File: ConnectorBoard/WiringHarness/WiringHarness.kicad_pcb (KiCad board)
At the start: 2 copper layers, 56.9 x 31.5 mm, 15 parts, among them J1 Barrel_Jack, J2 Conn_01x03, J3 Conn_01x03, J4 Conn_02x05_Odd_Even, U1 L7805, U2 L7805

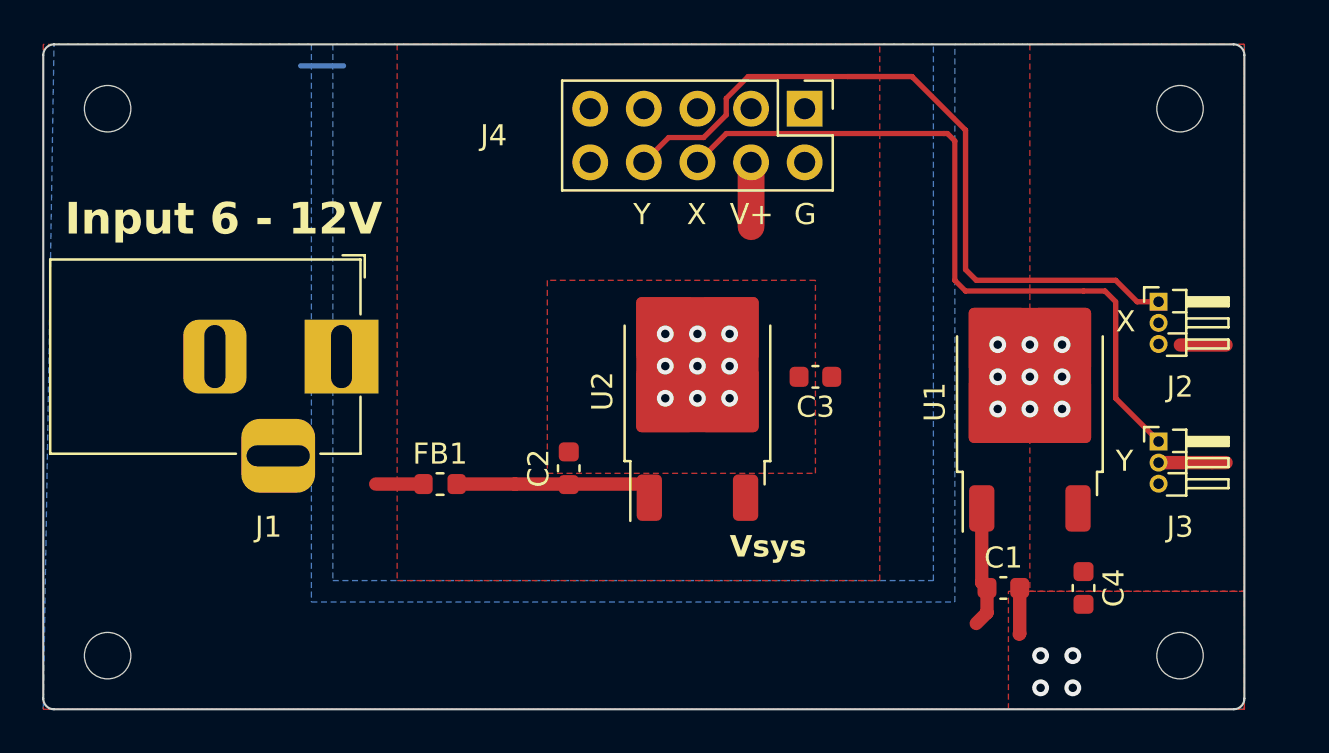
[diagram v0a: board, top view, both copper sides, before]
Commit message: Add right angle ribbon cable to wiring harness
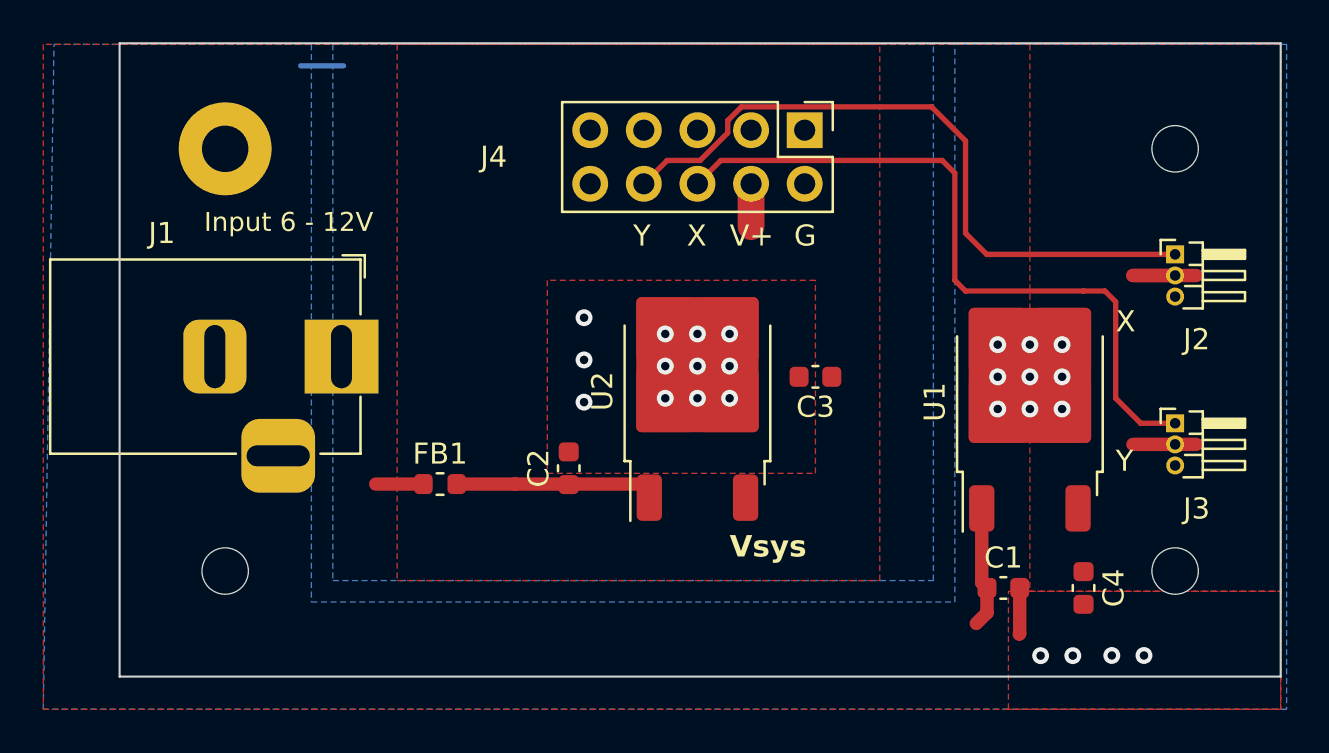
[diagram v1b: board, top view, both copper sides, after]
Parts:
- removed H1: MountingHole, MountingHole:MountingHole_2.2mm_M2
- added H5: MountingHole_Pad, MountingHole:MountingHole_2.2mm_M2_Pad, F.Cu at (160.0, 40.0)
- moved H2 56.0 mm to (205.0, 40.0)
- moved H4 45.4 mm to (160.0, 60.0)
- moved H3 21.9 mm to (205.0, 60.0)
- moved J2 2.38 mm to (205.0, 45.0)
- moved J3 1.17 mm to (205.0, 53.0)
- moved J4 1.02 mm to (187.5, 39.1)
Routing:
- net /VoutServo: track 5.36 -> 8.00 mm
- net /ServoY: track 34.8 -> 32.5 mm
- net /ServoX: track 35.0 -> 33.9 mm
- net /Vsys: track 3.05 -> 2.03 mm
- net GND: vias 22 -> 25
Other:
- board size 56.9 x 31.5 mm -> 55 x 30 mm

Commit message: Rounded corners and version string
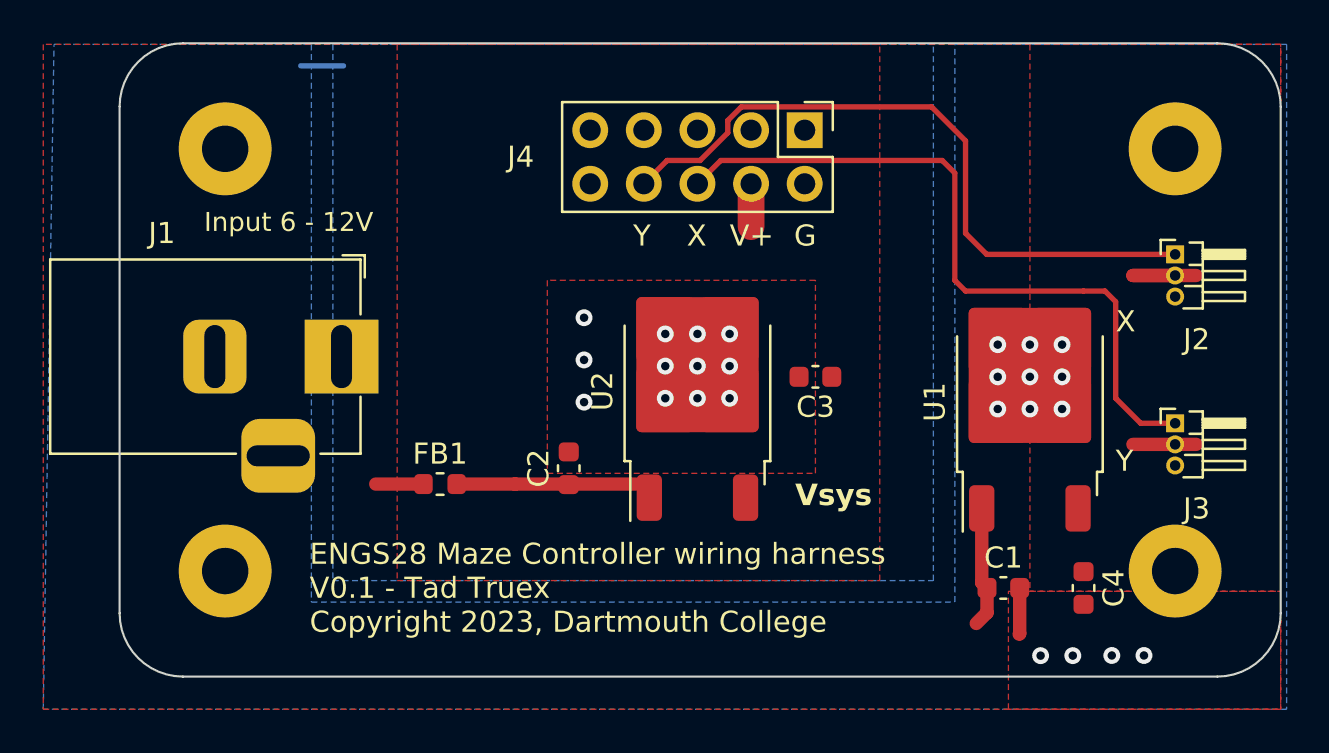
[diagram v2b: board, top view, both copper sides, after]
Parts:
- removed H4: MountingHole, MountingHole:MountingHole_2.2mm_M2
- added H1: MountingHole_Pad, MountingHole:MountingHole_2.2mm_M2_Pad, F.Cu at (205.0, 40.0)
- H2, H3: value MountingHole -> MountingHole_Pad; footprint MountingHole:MountingHole_2.2mm_M2 -> MountingHole:MountingHole_2.2mm_M2_Pad
- moved H3 45.0 mm to (160.0, 60.0)
- moved H2 20.0 mm to (205.0, 60.0)
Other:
- outline, holes or cut-outs redrawn
- board text added: "ENGS28 Maze Controller wiring harness V0.1 - Tad Truex Copyright 2023, Dartmouth College"
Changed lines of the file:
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@@
     )
-  )
-  (footprint "MountingHole:MountingHole_2.2mm_M2" (layer "F.Cu")
-    (at 205 60)
-    (descr "Mounting Hole 2.2mm, no annular, M2")
-    (tags "mounting hole 2.2mm no annular m2")
-    (property "Sheetfile" "WiringHarness.kicad_sch")
-    (property "Sheetname" "")
-    (property "ki_description" "Mounting Hole without connection")
-    (property "ki_keywords" "mounting hole")
-    (attr exclude_from_pos_files)
-    (fp_text reference "H3" (at 0 -3.2) (layer "F.SilkS") hide
-        (effects (font (size 1 1) (thickness 0.15)))
-    )
-    (fp_text value "MountingHole" (at 0 3.2) (layer "F.Fab")
-        (effects (font (size 1 1) (thickness 0.15)))
-    )
-    (fp_text user "${REFERENCE}" (at 0 0) (layer "F.Fab")
-        (effects (font (size 1 1) (thickness 0.15)))
-    )
-    (fp_circle (center 0 0) (end 2.2 0)
-      (stroke (width 0.15) (type solid)) (fill none) (layer "Cmts.User"))
-    (fp_circle (center 0 0) (end 2.45 0)
-      (stroke (width 0.05) (type solid)) (fill none) (layer "F.CrtYd"))
-    (pad "" np_thru_hole circle (at 0 0) (size 2.2 2.2) (drill 2.2) (layers "*.Cu" "*.Mask"))
   )
   (footprint "Capacitor_SMD:C_0603_1608Metric" (layer "F.Cu")
@@
     )
   )
-  (footprint "MountingHole:MountingHole_2.2mm_M2" (layer "F.Cu")
-    (at 205 40)
-    (descr "Mounting Hole 2.2mm, no annular, M2")
-    (tags "mounting hole 2.2mm no annular m2")
-    (property "Sheetfile" "WiringHarness.kicad_sch")
-    (property "Sheetname" "")
-    (property "ki_description" "Mounting Hole without connection")
+  (footprint "MountingHole:MountingHole_2.2mm_M2_Pad" (layer "F.Cu")
+    (at 160 60)
+    (descr "Mounting Hole 2.2mm, M2")
+    (tags "mounting hole 2.2mm m2")
+    (property "Sheetfile" "WiringHarness.kicad_sch")
+    (property "Sheetname" "")
+    (property "ki_description" "Mounting Hole with connection")
     (property "ki_keywords" "mounting hole")
     (attr exclude_from_pos_files)
-    (fp_text reference "H2" (at 0 -3.2) (layer "F.SilkS") hide
-        (effects (font (size 1 1) (thickness 0.15)))
-    )
-    (fp_text value "MountingHole" (at 0 3.2) (layer "F.Fab")
+    (fp_text reference "H3" (at 0 -3.2) (layer "F.SilkS") hide
+        (effects (font (size 1 1) (thickness 0.15)))
+    )
+    (fp_text value "MountingHole_Pad" (at 0 3.2) (layer "F.Fab") hide
         (effects (font (size 1 1) (thickness 0.15)))
     )
@@
     (fp_circle (center 0 0) (end 2.45 0)
       (stroke (width 0.05) (type solid)) (fill none) (layer "F.CrtYd"))
-    (pad "" np_thru_hole circle (at 0 0) (size 2.2 2.2) (drill 2.2) (layers "*.Cu" "*.Mask"))
+    (pad "1" thru_hole circle (at 0 0) (size 4.4 4.4) (drill 2.2) (layers "*.Cu" "*.Mask")
+      (net 2 "GND") (pinfunction "1") (pintype "input"))
   )
   (footprint "Connector_PinHeader_1.00mm:PinHeader_1x03_P1.00mm_Horizontal" (layer "F.Cu")
@@
     )
   )
+  (footprint "MountingHole:MountingHole_2.2mm_M2_Pad" (layer "F.Cu")
+    (at 205 60)
+    (descr "Mounting Hole 2.2mm, M2")
+    (tags "mounting hole 2.2mm m2")
+    (property "Sheetfile" "WiringHarness.kicad_sch")
+    (property "Sheetname" "")
+    (property "ki_description" "Mounting Hole with connection")
+    (property "ki_keywords" "mounting hole")
+    (attr exclude_from_pos_files)
+    (fp_text reference "H2" (at 0 -3.2) (layer "F.SilkS") hide
+        (effects (font (size 1 1) (thickness 0.15)))
+    )
+    (fp_text value "MountingHole_Pad" (at 0 3.2) (layer "F.Fab") hide
+        (effects (font (size 1 1) (thickness 0.15)))
+    )
+    (fp_text user "${REFERENCE}" (at 0 0) (layer "F.Fab")
+        (effects (font (size 1 1) (thickness 0.15)))
+    )
+    (fp_circle (center 0 0) (end 2.2 0)
+      (stroke (width 0.15) (type solid)) (fill none) (layer "Cmts.User"))
+    (fp_circle (center 0 0) (end 2.45 0)
+      (stroke (width 0.05) (type solid)) (fill none) (layer "F.CrtYd"))
+    (pad "1" thru_hole circle (at 0 0) (size 4.4 4.4) (drill 2.2) (layers "*.Cu" "*.Mask")
+      (net 2 "GND") (pinfunction "1") (pintype "input"))
+  )
   (footprint "Connector_PinHeader_2.54mm:PinHeader_2x05_P2.54mm_Vertical" (layer "F.Cu")
     (at 187.452 39.116 -90)
@@
     (property "ki_keywords" "connector")
     (attr through_hole)
-    (fp_text reference "J4" (at 1.27 14.732) (layer "F.SilkS")
+    (fp_text reference "J4" (at 1.27 13.452) (layer "F.SilkS")
         (effects (font (size 1 1) (thickness 0.15)))
     )
@@
     )
   )
+  (footprint "MountingHole:MountingHole_2.2mm_M2_Pad" (layer "F.Cu")
+    (at 205 40)
+    (descr "Mounting Hole 2.2mm, M2")
+    (tags "mounting hole 2.2mm m2")
+    (property "Sheetfile" "WiringHarness.kicad_sch")
+    (property "Sheetname" "")
+    (property "ki_description" "Mounting Hole with connection")
+    (property "ki_keywords" "mounting hole")
+    (attr exclude_from_pos_files)
+    (fp_text reference "H1" (at 0 -3.2) (layer "F.SilkS") hide
+        (effects (font (size 1 1) (thickness 0.15)))
+    )
+    (fp_text value "MountingHole_Pad" (at 0 3.2) (layer "F.Fab") hide
+        (effects (font (size 1 1) (thickness 0.15)))
+    )
+    (fp_text user "${REFERENCE}" (at 0 0) (layer "F.Fab")
+        (effects (font (size 1 1) (thickness 0.15)))
+    )
+    (fp_circle (center 0 0) (end 2.2 0)
+      (stroke (width 0.15) (type solid)) (fill none) (layer "Cmts.User"))
+    (fp_circle (center 0 0) (end 2.45 0)
+      (stroke (width 0.05) (type solid)) (fill none) (layer "F.CrtYd"))
+    (pad "1" thru_hole circle (at 0 0) (size 4.4 4.4) (drill 2.2) (layers "*.Cu" "*.Mask")
+      (net 2 "GND") (pinfunction "1") (pintype "input"))
+  )
   (footprint "Capacitor_SMD:C_0603_1608Metric" (layer "F.Cu")
     (at 200.661 60.802 -90)
@@
     )
   )
-  (footprint "MountingHole:MountingHole_2.2mm_M2" (layer "F.Cu")
-    (at 160 60)
-    (descr "Mounting Hole 2.2mm, no annular, M2")
-    (tags "mounting hole 2.2mm no annular m2")
-    (property "Sheetfile" "WiringHarness.kicad_sch")
-    (property "Sheetname" "")
-    (property "ki_description" "Mounting Hole without connection")
-    (property "ki_keywords" "mounting hole")
-    (attr exclude_from_pos_files)
-    (fp_text reference "H4" (at 0 -3.2) (layer "F.SilkS") hide
-        (effects (font (size 1 1) (thickness 0.15)))
-    )
-    (fp_text value "MountingHole" (at 0 3.2) (layer "F.Fab")
-        (effects (font (size 1 1) (thickness 0.15)))
-    )
-    (fp_text user "${REFERENCE}" (at 0 0) (layer "F.Fab")
-        (effects (font (size 1 1) (thickness 0.15)))
-    )
-    (fp_circle (center 0 0) (end 2.2 0)
-      (stroke (width 0.15) (type solid)) (fill none) (layer "Cmts.User"))
-    (fp_circle (center 0 0) (end 2.45 0)
-      (stroke (width 0.05) (type solid)) (fill none) (layer "F.CrtYd"))
-    (pad "" np_thru_hole circle (at 0 0) (size 2.2 2.2) (drill 2.2) (layers "*.Cu" "*.Mask"))
-  )
   (footprint "Inductor_SMD:L_0603_1608Metric" (layer "F.Cu")
     (at 170.18 55.88)
@@
     )
   )
-  (gr_line (start 155 65) (end 210 65)
+  (gr_arc (start 155 38) (mid 155.87868 35.87868) (end 158 35)
     (stroke (width 0.1) (type default)) (layer "Edge.Cuts"))
-  (gr_line (start 210 35) (end 155 35)
+  (gr_line (start 158 65) (end 207 65)
     (stroke (width 0.1) (type default)) (layer "Edge.Cuts"))
-  (gr_line (start 155 35) (end 155 65)
+  (gr_arc (start 210 62) (mid 209.12132 64.12132) (end 207 65)
     (stroke (width 0.1) (type default)) (layer "Edge.Cuts"))
-  (gr_line (start 210 65) (end 210 35)
+  (gr_line (start 207 35) (end 158 35)
+    (stroke (width 0.1) (type default)) (layer "Edge.Cuts"))
+  (gr_line (start 155 38) (end 155 62)
+    (stroke (width 0.1) (type default)) (layer "Edge.Cuts"))
+  (gr_arc (start 158 65) (mid 155.87868 64.12132) (end 155 62)
+    (stroke (width 0.1) (type default)) (layer "Edge.Cuts"))
+  (gr_arc (start 207 35) (mid 209.12132 35.87868) (end 210 38)
+    (stroke (width 0.1) (type default)) (layer "Edge.Cuts"))
+  (gr_line (start 210 62) (end 210 38)
     (stroke (width 0.1) (type default)) (layer "Edge.Cuts"))
   (gr_text "G" (at 186.944 44.704) (layer "F.SilkS")
@@
     (effects (font (size 1 1) (thickness 0.15)) (justify left bottom))
   )
-  (gr_text "Vsys" (at 183.896 59.436) (layer "F.SilkS")
+  (gr_text "Vsys" (at 187 57) (layer "F.SilkS")
     (effects (font (size 1.016 1.016) (thickness 0.127) bold) (justify left bottom))
   )
@@
     (effects (font (size 0.9 0.9) (thickness 0.09)) (justify left bottom))
   )
+  (gr_text "ENGS28 Maze Controller wiring harness\nV0.1 - Tad Truex\nCopyright 2023, Dartmouth College\n" (at 164 63) (layer "F.SilkS")
+    (effects (font (size 1 1) (thickness 0.15)) (justify left bottom))
+  )
   (segment (start 196.088 60.802) (end 196.088 61.976) (width 0.635) (layer "F.Cu") (net 1))

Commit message: Add QR code
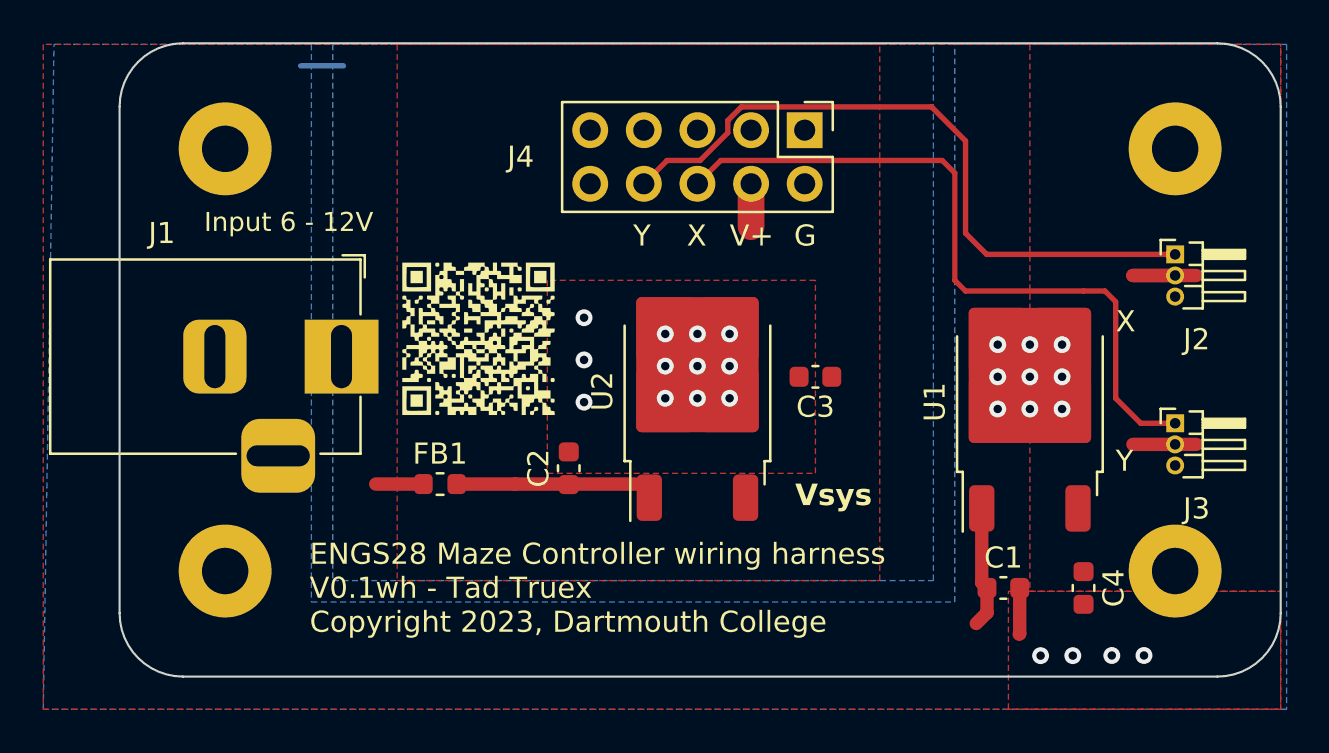
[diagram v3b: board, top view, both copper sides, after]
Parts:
- added G***: LOGO, QRCodeLibrary:v0.1wh, F.Cu at (172.0, 49.0)
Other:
- board text added: "ENGS28 Maze Controller wiring harness V0.1wh - Tad Truex Copyright 2023, Dartmouth College"
- board text removed: "ENGS28 Maze Controller wiring harness V0.1 - Tad Truex Copyright 2023, Dartmouth College"
